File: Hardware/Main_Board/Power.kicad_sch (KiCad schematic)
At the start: 1 part, among them U2 LM2596DSADJG

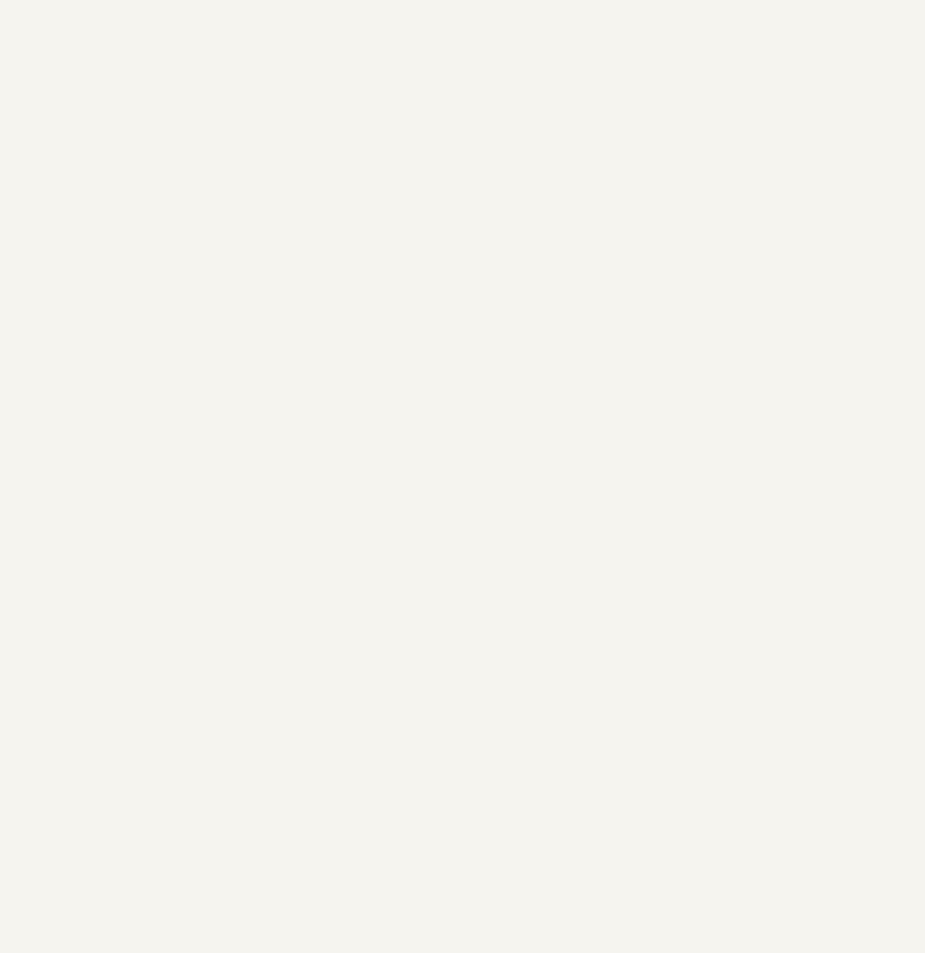
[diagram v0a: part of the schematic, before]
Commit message: Mixed in all of Layth's work, and added extra sheets
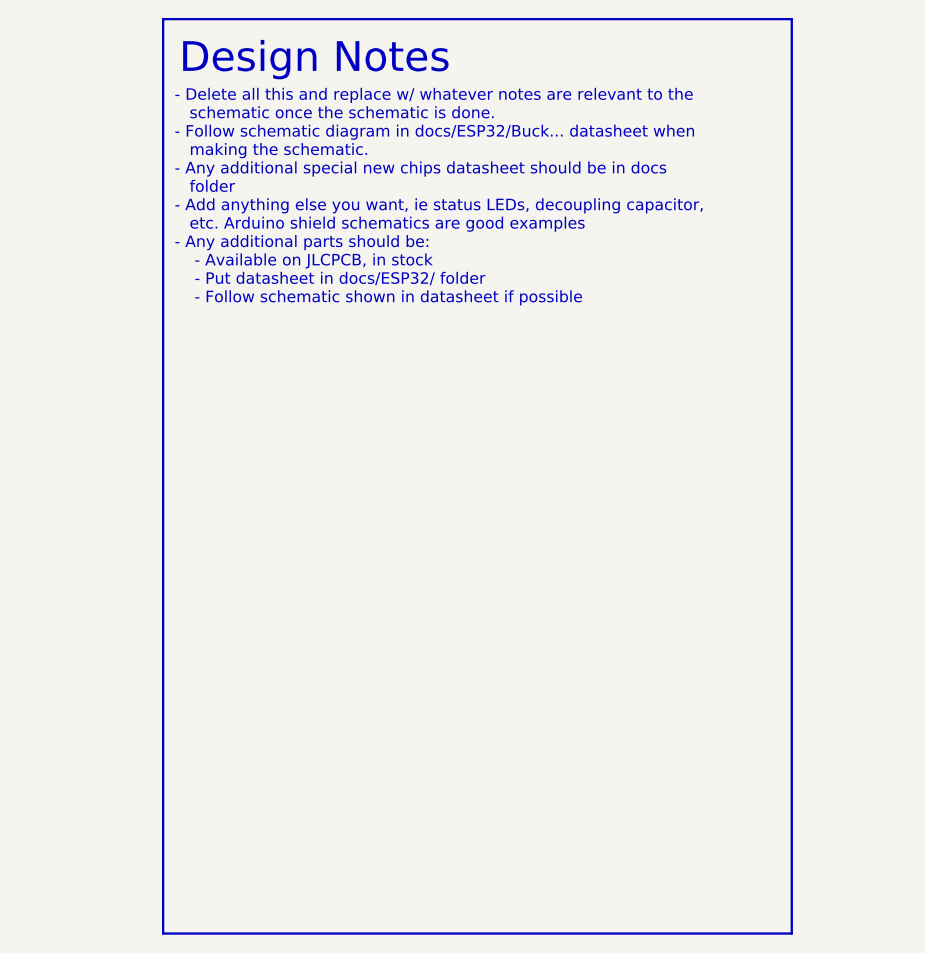
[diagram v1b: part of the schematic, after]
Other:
- note added: "- Delete all this and replace w/ whatever notes are relevant to the schematic once the schematic is done. - Follow schematic diagram in docs/ESP32/Buck... datasheet when making the schematic. - Any additional special new chips datasheet should be in docs folder - Add anything else you want, ie status LEDs, decoupling capacitor, etc. Arduino shield schematics are good examples - Any additional par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"
- note added: "Design Notes"
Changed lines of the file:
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@@
 	(generator_version "9.0")
 	(paper "A4")
+	(rectangle
+		(start 212.09 15.24)
+		(end 281.94 116.84)
+		(stroke
+			(width 0.254)
+			(type solid)
+		)
+		(fill
+			(type none)
+		)
+	)
+	(text "Design Notes"
+		(exclude_from_sim no)
+		(at 213.868 17.78 0)
+		(effects
+			(font
+				(size 3.302 3.302)
+				(thickness 0.4128)
+			)
+			(justify left top)
+		)
+	)
+	(text "- Delete all this and replace w/ whatever notes are relevant to the\n   schematic once the schematic is done.\n- Follow schematic diagram in docs/ESP32/Buck... datasheet when\n   making the schematic.\n- Any additional special new chips datasheet should be in docs\n   folder\n- Add anything else you want, ie status LEDs, decoupling capacitor,\n   etc. Arduino shield schematics are good examples\n- Any additional parts should be:\n    - Available on JLCPCB, in stock\n    - Put datasheet in docs/ESP32/ folder\n	- Follow schematic shown in datasheet if possible"
+		(exclude_from_sim no)
+		(at 213.36 23.114 0)
+		(effects
+			(font
+				(size 1.27 1.27)
+			)
+			(justify left top)
+		)
+	)
 	(symbol
 		(lib_id "ESP32-Symbols:LM2596DSADJG")

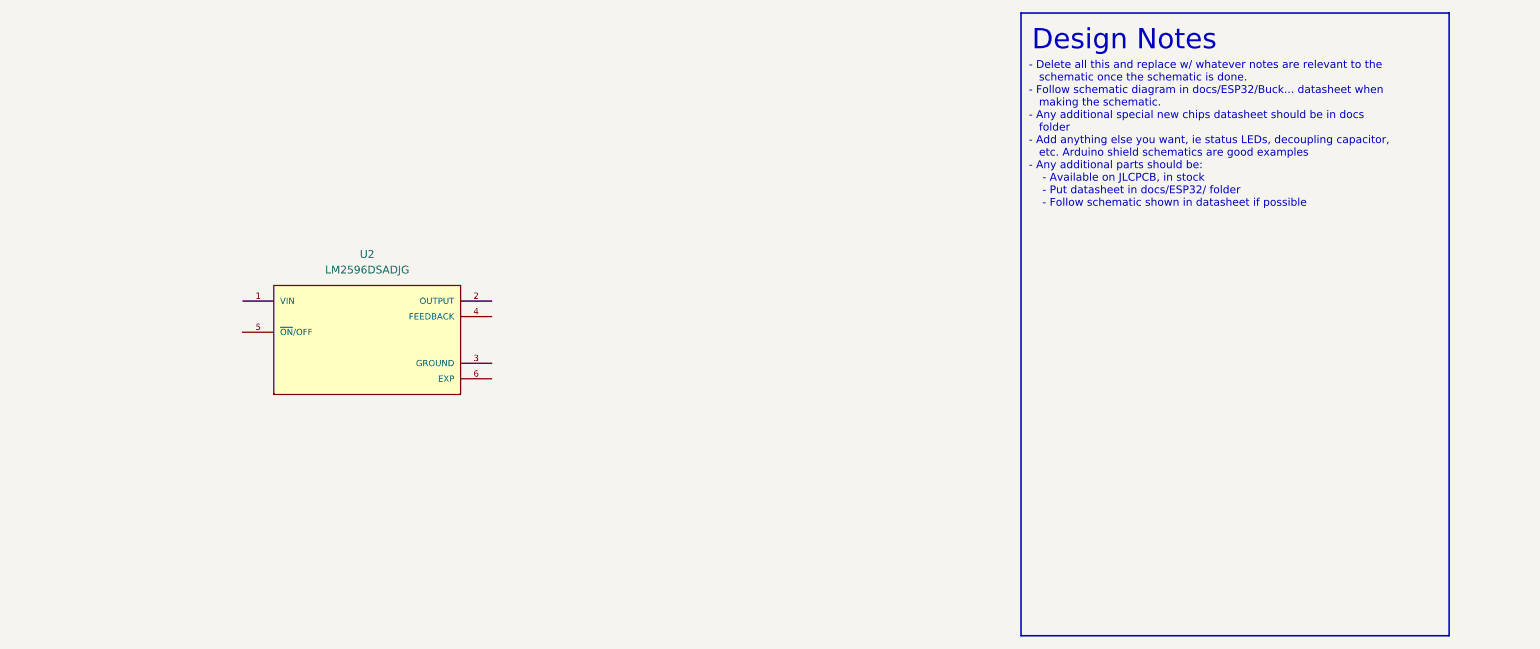
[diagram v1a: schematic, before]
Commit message: On behalf of Panuha and Layth: Added inital schematics for Main Board
- Added initial power units, 3v3 LDO remains
- Added buses for the ESP, UWB, and STM boards
- Connector sheet, footprint assignment, ERC check, etc remains.
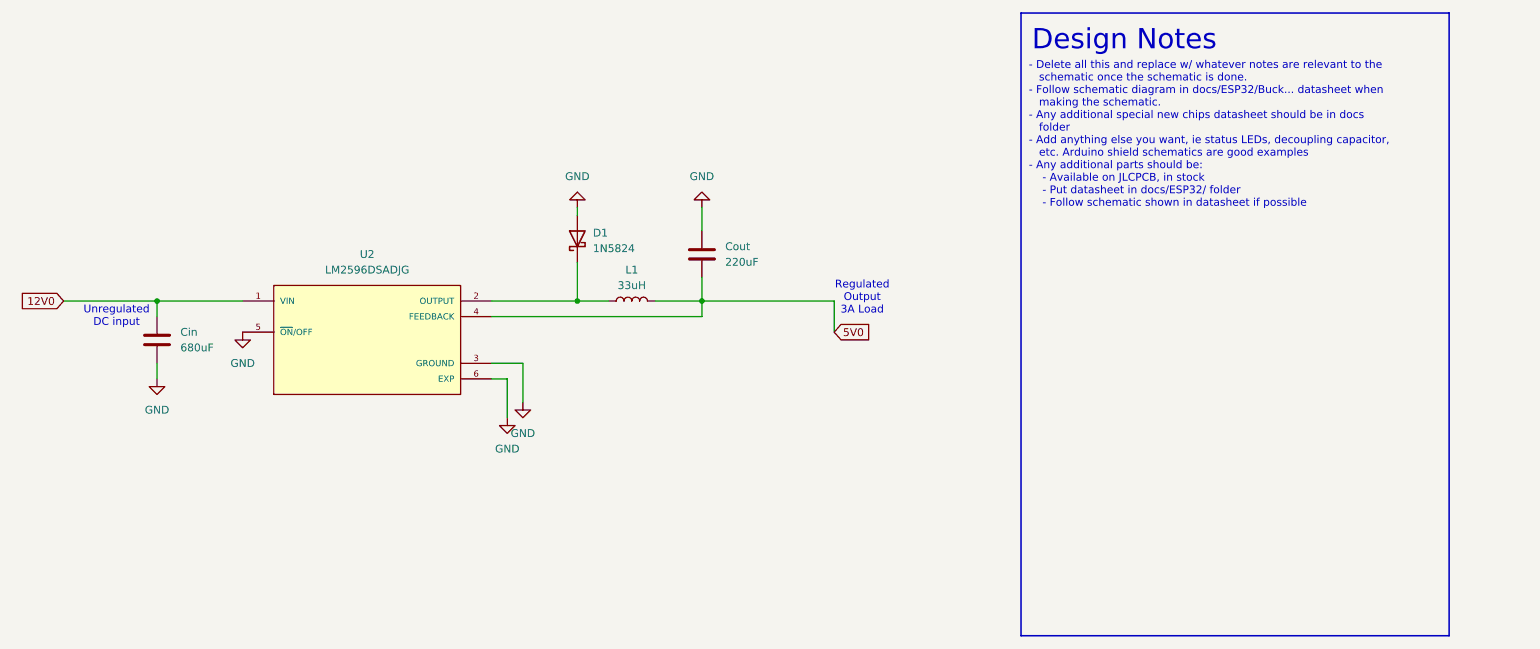
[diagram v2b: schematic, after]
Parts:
- added Cin: 680uF, symbol Device:C
- added Cout: 220uF, symbol Device:C
- added D1: 1N5824, Diode_THT:D_DO-201AD_P15.24mm_Horizontal, symbol Diode:1N5822
- added L1: 33uH, symbol Device:L
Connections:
- net 12V0: now reaches U2.1 (VIN)
- net 12V0: now also Cin.1
- net at U2.2 (OUTPUT): now also D1.1 (K), L1.1
- net GND: now reaches U2.3 (GROUND)
- net GND: now also U2.5 (~{ON}/OFF), U2.6 (EXP), Cin.2, Cout.1, D1.2 (A)
- net 5V0: now reaches U2.4 (FEEDBACK)
- net 5V0: now also Cout.2, L1.2
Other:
- note added: "Regulated Output 3A Load"
- note added: "Unregulated DC input"
